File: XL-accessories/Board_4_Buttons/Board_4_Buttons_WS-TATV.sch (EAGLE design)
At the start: 1 part

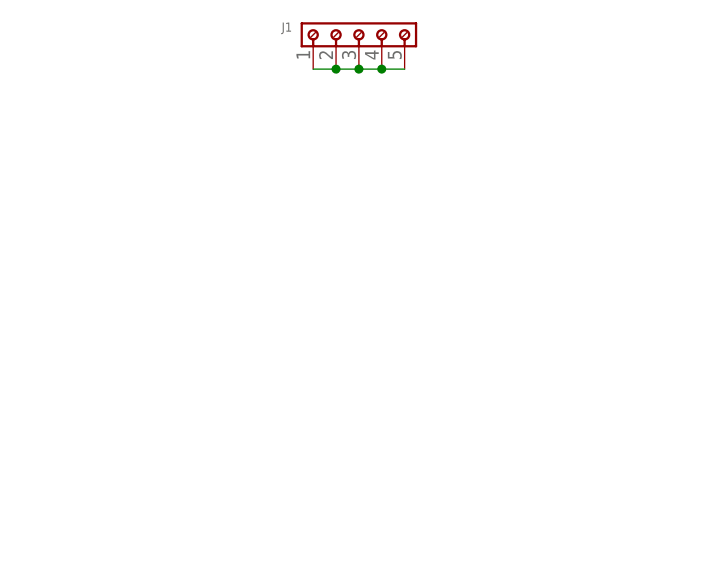
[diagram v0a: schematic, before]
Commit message: Update grid settings and layer visibility, modify library descriptions, and adjust package details.
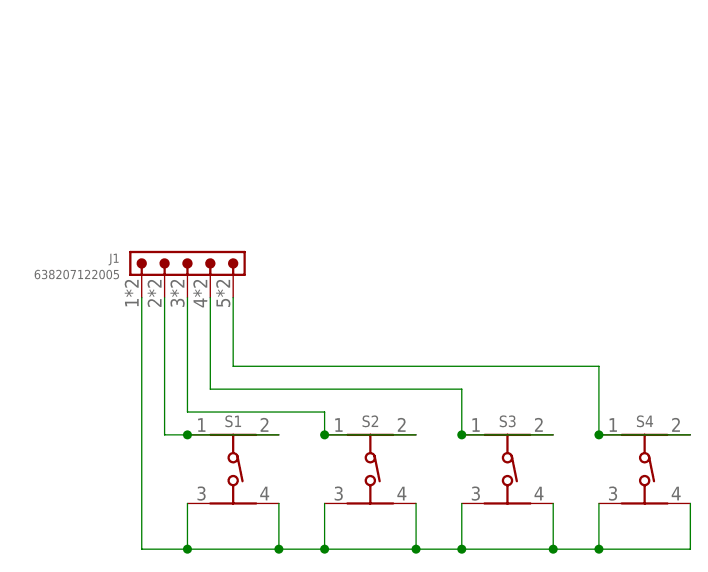
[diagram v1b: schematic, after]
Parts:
- added S1, S2, S3, S4: (no value), Wurth_Switch_WS-TATV:430456073736
- J1: value (none) -> 638207122005; device Wurth_Connectors_WR-TBL Rising Cage Clamp:691508110305 -> Wurth_Connectors_WR-FAST:638207122005
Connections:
- new net N$5: J1.2, S1.1, S1.3
- new net N$6: J1.3, S2.1, S2.3
- new net N$7: J1.4, S3.1, S3.3
- new net N$8: J1.5, S4.1, S4.3
- net N$1: now also S1.2, S1.4, S2.2, S2.4, S3.2, S3.4, S4.2, S4.4; no longer J1.2, J1.3, J1.4, J1.5
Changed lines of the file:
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@@
 <layers>
 <layer number="1" name="Top" color="4" fill="1" visible="no" active="no"/>
+<layer number="2" name="Route2" color="1" fill="3" visible="no" active="no"/>
+<layer number="3" name="Route3" color="4" fill="3" visible="no" active="no"/>
+<layer number="4" name="Route4" color="1" fill="4" visible="no" active="no"/>
+<layer number="5" name="Route5" color="4" fill="4" visible="no" active="no"/>
+<layer number="6" name="Route6" color="1" fill="8" visible="no" active="no"/>
+<layer number="7" name="Route7" color="4" fill="8" visible="no" active="no"/>
+<layer number="8" name="Route8" color="1" fill="2" visible="no" active="no"/>
+<layer number="9" name="Route9" color="4" fill="2" visible="no" active="no"/>
+<layer number="10" name="Route10" color="1" fill="7" visible="no" active="no"/>
+<layer number="11" name="Route11" color="4" fill="7" visible="no" active="no"/>
+<layer number="12" name="Route12" color="1" fill="5" visible="no" active="no"/>
+<layer number="13" name="Route13" color="4" fill="5" visible="no" active="no"/>
+<layer number="14" name="Route14" color="1" fill="6" visible="no" active="no"/>
+<layer number="15" name="Route15" color="4" fill="6" visible="no" active="no"/>
 <layer number="16" name="Bottom" color="1" fill="1" visible="no" active="no"/>
 <layer number="17" name="Pads" color="2" fill="1" visible="no" active="no"/>
@@
 </classes>
 <parts>
-<part name="J1" library="Wurth_Connectors_WR-TBL Rising Cage Clamp" library_urn="urn:adsk.eagle:library:16280519" deviceset="691508110305" device="" package3d_urn="urn:adsk.eagle:package:16248440/3"/>
+<part name="S1" library="Wurth_Switch_WS-TATV" library_urn="urn:adsk.eagle:library:18256259" deviceset="430456073736" device="" package3d_urn="urn:adsk.eagle:package:18256273/2"/>
+<part name="S2" library="Wurth_Switch_WS-TATV" library_urn="urn:adsk.eagle:library:18256259" deviceset="430456073736" device="" package3d_urn="urn:adsk.eagle:package:18256273/2"/>
+<part name="S3" library="Wurth_Switch_WS-TATV" library_urn="urn:adsk.eagle:library:18256259" deviceset="430456073736" device="" package3d_urn="urn:adsk.eagle:package:18256273/2"/>
+<part name="S4" library="Wurth_Switch_WS-TATV" library_urn="urn:adsk.eagle:library:18256259" deviceset="430456073736" device="" package3d_urn="urn:adsk.eagle:package:18256273/2"/>
+<part name="J1" library="Wurth_Connectors_WR-FAST" library_urn="urn:adsk.eagle:library:15267884" deviceset="638207122005" device="" package3d_urn="urn:adsk.eagle:package:15267967/3" value=" 638207122005 "/>
 </parts>
 <sheets>
@@
 </plain>
 <instances>
-<instance part="J1" gate="G$1" x="36.83" y="71.12" smashed="yes">
-<attribute name="NAME" x="29.41" y="70.198" size="1.016" layer="95" align="bottom-right"/>
-<attribute name="VALUE" x="29.46" y="68.54" size="1.016" layer="96" align="bottom-right"/>
+<instance part="S1" gate="G$1" x="22.86" y="20.32" smashed="yes">
+<attribute name="NAME" x="22.89" y="26.27" size="1.27" layer="95" align="bottom-center"/>
+<attribute name="VALUE" x="19.15" y="15.94" size="1.27" layer="96"/>
+</instance>
+<instance part="S2" gate="G$1" x="38.1" y="20.32" smashed="yes">
+<attribute name="NAME" x="38.13" y="26.27" size="1.27" layer="95" align="bottom-center"/>
+<attribute name="VALUE" x="34.39" y="15.94" size="1.27" layer="96"/>
+</instance>
+<instance part="S3" gate="G$1" x="53.34" y="20.32" smashed="yes">
+<attribute name="NAME" x="53.37" y="26.27" size="1.27" layer="95" align="bottom-center"/>
+<attribute name="VALUE" x="49.63" y="15.94" size="1.27" layer="96"/>
+</instance>
+<instance part="S4" gate="G$1" x="68.58" y="20.32" smashed="yes">
+<attribute name="NAME" x="68.61" y="26.27" size="1.27" layer="95" align="bottom-center"/>
+<attribute name="VALUE" x="64.87" y="15.94" size="1.27" layer="96"/>
+</instance>
+<instance part="J1" gate="G$1" x="17.78" y="45.72" smashed="yes">
+<attribute name="NAME" x="10.25" y="44.515" size="1.016" layer="95" align="bottom-right"/>
+<attribute name="VALUE" x="10.29" y="42.71" size="1.016" layer="96" align="bottom-right"/>
 </instance>
 </instances>
@@
 <segment>
 <pinref part="J1" gate="G$1" pin="1"/>
-<pinref part="J1" gate="G$1" pin="2"/>
-<wire x1="31.75" y1="66.04" x2="34.29" y2="66.04" width="0.1524" layer="91"/>
-<pinref part="J1" gate="G$1" pin="3"/>
-<wire x1="36.83" y1="66.04" x2="34.29" y2="66.04" width="0.1524" layer="91"/>
-<junction x="34.29" y="66.04"/>
-<pinref part="J1" gate="G$1" pin="4"/>
-<wire x1="39.37" y1="66.04" x2="36.83" y2="66.04" width="0.1524" layer="91"/>
-<junction x="36.83" y="66.04"/>
-<pinref part="J1" gate="G$1" pin="5"/>
-<wire x1="41.91" y1="66.04" x2="39.37" y2="66.04" width="0.1524" layer="91"/>
-<junction x="39.37" y="66.04"/>
+<wire x1="12.7" y1="40.64" x2="12.7" y2="12.7" width="0.1524" layer="91"/>
+<pinref part="S4" gate="G$1" pin="4"/>
+<wire x1="12.7" y1="12.7" x2="17.78" y2="12.7" width="0.1524" layer="91"/>
+<wire x1="17.78" y1="12.7" x2="27.94" y2="12.7" width="0.1524" layer="91"/>
+<wire x1="27.94" y1="12.7" x2="33.02" y2="12.7" width="0.1524" layer="91"/>
+<wire x1="33.02" y1="12.7" x2="43.18" y2="12.7" width="0.1524" layer="91"/>
+<wire x1="43.18" y1="12.7" x2="48.26" y2="12.7" width="0.1524" layer="91"/>
+<wire x1="48.26" y1="12.7" x2="58.42" y2="12.7" width="0.1524" layer="91"/>
+<wire x1="58.42" y1="12.7" x2="63.5" y2="12.7" width="0.1524" layer="91"/>
+<wire x1="63.5" y1="12.7" x2="73.66" y2="12.7" width="0.1524" layer="91"/>
+<wire x1="73.66" y1="12.7" x2="73.66" y2="17.78" width="0.1524" layer="91"/>
+<pinref part="S4" gate="G$1" pin="2"/>
+<wire x1="63.5" y1="17.78" x2="63.5" y2="12.7" width="0.1524" layer="91"/>
+<junction x="63.5" y="12.7"/>
+<pinref part="S3" gate="G$1" pin="2"/>
+<wire x1="48.26" y1="17.78" x2="48.26" y2="12.7" width="0.1524" layer="91"/>
+<junction x="48.26" y="12.7"/>
+<pinref part="S2" gate="G$1" pin="2"/>
+<wire x1="33.02" y1="17.78" x2="33.02" y2="12.7" width="0.1524" layer="91"/>
+<junction x="33.02" y="12.7"/>
+<pinref part="S2" gate="G$1" pin="4"/>
+<wire x1="43.18" y1="17.78" x2="43.18" y2="12.7" width="0.1524" layer="91"/>
+<junction x="43.18" y="12.7"/>
+<pinref part="S1" gate="G$1" pin="4"/>
+<wire x1="27.94" y1="17.78" x2="27.94" y2="12.7" width="0.1524" layer="91"/>
+<junction x="27.94" y="12.7"/>
+<pinref part="S1" gate="G$1" pin="2"/>
+<wire x1="17.78" y1="17.78" x2="17.78" y2="12.7" width="0.1524" layer="91"/>
+<junction x="17.78" y="12.7"/>
+<pinref part="S3" gate="G$1" pin="4"/>
+<wire x1="58.42" y1="17.78" x2="58.42" y2="12.7" width="0.1524" layer="91"/>
+<junction x="58.42" y="12.7"/>
 </segment>
 </net>
+<net name="N$5" class="0">
+<segment>
+<pinref part="S1" gate="G$1" pin="1"/>
+<pinref part="J1" gate="G$1" pin="2"/>
+<wire x1="17.78" y1="25.4" x2="15.24" y2="25.4" width="0.1524" layer="91"/>
+<wire x1="15.24" y1="25.4" x2="15.24" y2="40.64" width="0.1524" layer="91"/>
+<pinref part="S1" gate="G$1" pin="3"/>
+<wire x1="27.94" y1="25.4" x2="17.78" y2="25.4" width="0.1524" layer="91"/>
+<junction x="17.78" y="25.4"/>
+</segment>
+</net>
+<net name="N$6" class="0">
+<segment>
+<pinref part="S2" gate="G$1" pin="1"/>
+<wire x1="33.02" y1="25.4" x2="33.02" y2="27.94" width="0.1524" layer="91"/>
+<wire x1="33.02" y1="27.94" x2="17.78" y2="27.94" width="0.1524" layer="91"/>
+<pinref part="J1" gate="G$1" pin="3"/>
+<wire x1="17.78" y1="27.94" x2="17.78" y2="40.64" width="0.1524" layer="91"/>
+<pinref part="S2" gate="G$1" pin="3"/>
+<wire x1="43.18" y1="25.4" x2="33.02" y2="25.4" width="0.1524" layer="91"/>
+<junction x="33.02" y="25.4"/>
+</segment>
+</net>
+<net name="N$7" class="0">
+<segment>
+<pinref part="S3" gate="G$1" pin="1"/>
+<wire x1="48.26" y1="25.4" x2="48.26" y2="30.48" width="0.1524" layer="91"/>
+<wire x1="48.26" y1="30.48" x2="20.32" y2="30.48" width="0.1524" layer="91"/>
+<pinref part="J1" gate="G$1" pin="4"/>
+<wire x1="20.32" y1="30.48" x2="20.32" y2="40.64" width="0.1524" layer="91"/>
+<pinref part="S3" gate="G$1" pin="3"/>
+<wire x1="48.26" y1="25.4" x2="58.42" y2="25.4" width="0.1524" layer="91"/>
+<junction x="48.26" y="25.4"/>
+</segment>
+</net>
+<net name="N$8" class="0">
+<segment>
+<pinref part="S4" gate="G$1" pin="1"/>
+<wire x1="63.5" y1="25.4" x2="63.5" y2="33.02" width="0.1524" layer="91"/>
+<wire x1="63.5" y1="33.02" x2="22.86" y2="33.02" width="0.1524" layer="91"/>
+<pinref part="J1" gate="G$1" pin="5"/>
+<wire x1="22.86" y1="33.02" x2="22.86" y2="40.64" width="0.1524" layer="91"/>
+<pinref part="S4" gate="G$1" pin="3"/>
+<wire x1="63.5" y1="25.4" x2="73.66" y2="25.4" width="0.1524" layer="91"/>
+<junction x="63.5" y="25.4"/>
+</segment>
+</net>
